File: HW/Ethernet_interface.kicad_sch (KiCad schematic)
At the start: 52 parts, among them J1 ARJM11C7-114-BA-EW2, U10 AZ1117-3.3_SOT89, U3 W5500, U7 SN74LV1T125DCK, U8 SN74LV1T125DCK, U9 APX811-31UG-7, Y1 25Mhz

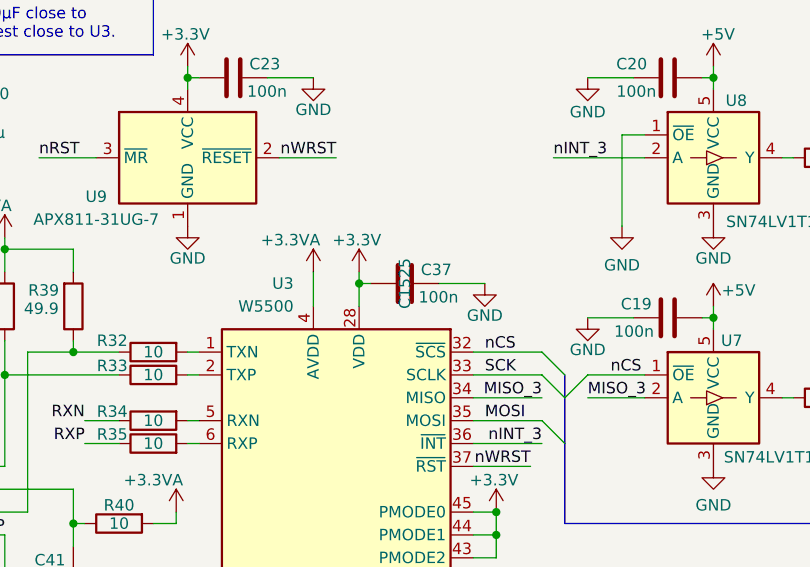
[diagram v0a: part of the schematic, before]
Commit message: Added uart and i2c to jtag connector, docs added
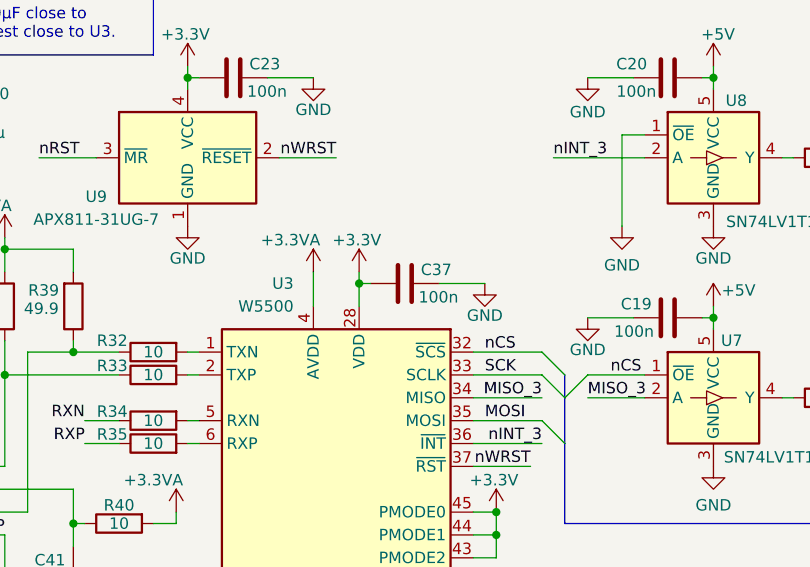
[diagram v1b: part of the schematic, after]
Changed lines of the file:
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@@
 (kicad_sch
-	(version 20241004)
+	(version 20241209)
 	(generator "eeschema")
 	(generator_version "8.99")
@@
 					(size 1.27 1.27)
 				)
+				(hide yes)
 			)
 		)
